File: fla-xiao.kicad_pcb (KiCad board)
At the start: 2 copper layers, 49.7 x 30.7 mm, 9 parts, among them J3 Conn_PinHeader_2x03_P2.54mm_V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, J4 Conn_PinHeader_1x08_P2.54mm_H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, J5 Conn_PinHeader_1x05_P2.54mm_H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, M1 Module_XIAO-RP2040_SocketSMD, SW1 BUTTON_B3SN

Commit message: Minor tweaks, updated image
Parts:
- moved R3 2.12 mm to (169.9, 150.7), turned to 0 degrees
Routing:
- net PWR_5V: track 52.5 -> 53.3 mm
- net PWR_3V3: track 114.2 -> 114.7 mm
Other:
- board size 49.7 x 30.7 mm -> 48.7 x 30.7 mm

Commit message: Fixed routing
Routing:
- net PWR_3V3: track 114.7 -> 115.3 mm
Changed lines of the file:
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@@
   (segment (start 164.979645 141.970355) (end 166.179199 141.970355) (width 0.6) (layer "F.Cu") (net 11))
   (segment (start 147.25 154) (end 145.39 152.14) (width 0.6) (layer "F.Cu") (net 12))
-  (segment (start 162 132.15) (end 162 134.035152) (width 0.6) (layer "F.Cu") (net 12))
-  (segment (start 168.9 129.35) (end 164.8 129.35) (width 0.6) (layer "F.Cu") (net 12))
+  (segment (start 162 134.035152) (end 161.404797 134.630355) (width 0.6) (layer "F.Cu") (net 12))
+  (segment (start 169.625 137.45) (end 169.625 129.775) (width 0.6) (layer "F.Cu") (net 12))
   (segment (start 148.675 130.625) (end 148.675 137.35) (width 0.6) (layer "F.Cu") (net 12))
   (segment (start 141.425 141.9) (end 143 141.9) (width 0.6) (layer "F.Cu") (net 12))
-  (segment (start 168.625 137.505) (end 168.625 145.85) (width 0.6) (layer "F.Cu") (net 12))
   (segment (start 168.504645 145.970355) (end 168.625 145.85) (width 0.6) (layer "F.Cu") (net 12))
   (segment (start 140.725 139.05) (end 140.725 141.2) (width 0.6) (layer "F.Cu") (net 12))
   (segment (start 147.725 138.3) (end 141.475 138.3) (width 0.6) (layer "F.Cu") (net 12))
   (segment (start 168.4 154) (end 147.25 154) (width 0.6) (layer "F.Cu") (net 12))
-  (segment (start 169.075 129.525) (end 168.9 129.35) (width 0.6) (layer "F.Cu") (net 12))
+  (segment (start 164.8 129.35) (end 162 132.15) (width 0.6) (layer "F.Cu") (net 12))
   (segment (start 145.39 150.9) (end 145.39 151.335) (width 0.6) (layer "F.Cu") (net 12))
   (segment (start 145.39 150.5) (end 145.39 150.9) (width 0.6) (layer "F.Cu") (net 12))
   (segment (start 148.675 137.35) (end 147.725 138.3) (width 0.6) (layer "F.Cu") (net 12))
   (segment (start 168.6125 148.3375) (end 169.8 149.525) (width 0.6) (layer "F.Cu") (net 12))
-  (segment (start 168.625 137.505) (end 169.075 137.055) (width 0.6) (layer "F.Cu") (net 12))
-  (segment (start 162 134.035152) (end 161.404797 134.630355) (width 0.6) (layer "F.Cu") (net 12))
   (segment (start 145.39 152.14) (end 145.39 150.9) (width 0.6) (layer "F.Cu") (net 12))
   (segment (start 168.625 148.325) (end 168.6125 148.3375) (width 0.6) (layer "F.Cu") (net 12))
   (segment (start 161.404799 134.630355) (end 161.414296 134.639854) (width 0.6) (layer "F.Cu") (net 12))
   (segment (start 141.475 138.3) (end 140.725 139.05) (width 0.6) (layer "F.Cu") (net 12))
-  (segment (start 164.8 129.35) (end 162 132.15) (width 0.6) (layer "F.Cu") (net 12))
   (segment (start 169.8 152.6) (end 168.4 154) (width 0.6) (layer "F.Cu") (net 12))
-  (segment (start 169.075 137.055) (end 169.075 129.525) (width 0.6) (layer "F.Cu") (net 12))
+  (segment (start 168.625 138.45) (end 169.625 137.45) (width 0.6) (layer "F.Cu") (net 12))
   (segment (start 133.495 134.88) (end 140.3 128.075) (width 0.6) (layer "F.Cu") (net 12))
   (segment (start 161.395298 134.639854) (end 161.404799 134.630355) (width 0.6) (layer "F.Cu") (net 12))
+  (segment (start 162 132.15) (end 162 134.035152) (width 0.6) (layer "F.Cu") (net 12))
   (segment (start 140.3 128.075) (end 146.125 128.075) (width 0.6) (layer "F.Cu") (net 12))
+  (segment (start 169.625 129.775) (end 169.2 129.35) (width 0.6) (layer "F.Cu") (net 12))
   (segment (start 140.725 141.2) (end 141.425 141.9) (width 0.6) (layer "F.Cu") (net 12))
   (segment (start 168.625 145.85) (end 168.625 148.325) (width 0.6) (layer "F.Cu") (net 12))
@@
   (segment (start 166.179199 145.970355) (end 168.504645 145.970355) (width 0.6) (layer "F.Cu") (net 12))
   (segment (start 132.7 134.88) (end 133.495 134.88) (width 0.6) (layer "F.Cu") (net 12))
+  (segment (start 169.2 129.35) (end 164.8 129.35) (width 0.6) (layer "F.Cu") (net 12))
   (segment (start 146.125 128.075) (end 148.675 130.625) (width 0.6) (layer "F.Cu") (net 12))
+  (segment (start 168.625 145.85) (end 168.625 138.45) (width 0.6) (layer "F.Cu") (net 12))
   (segment (start 139.375 126.8) (end 147.225 126.8) (width 0.6) (layer "F.Cu") (net 13))
   (segment (start 161.404797 129.550355) (end 160.825 130.130152) (width 0.6) (layer "F.Cu") (net 13))

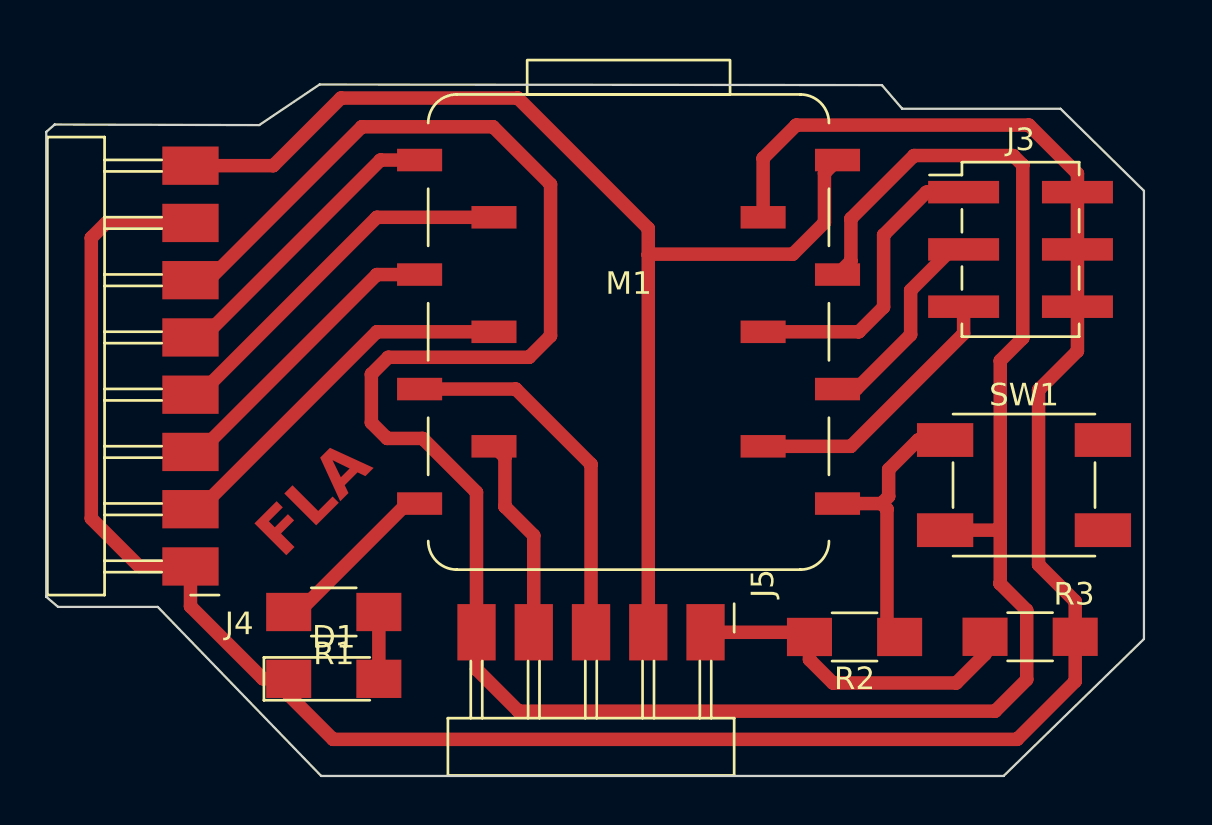
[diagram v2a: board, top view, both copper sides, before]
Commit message: Updated design, for Xtool Laser
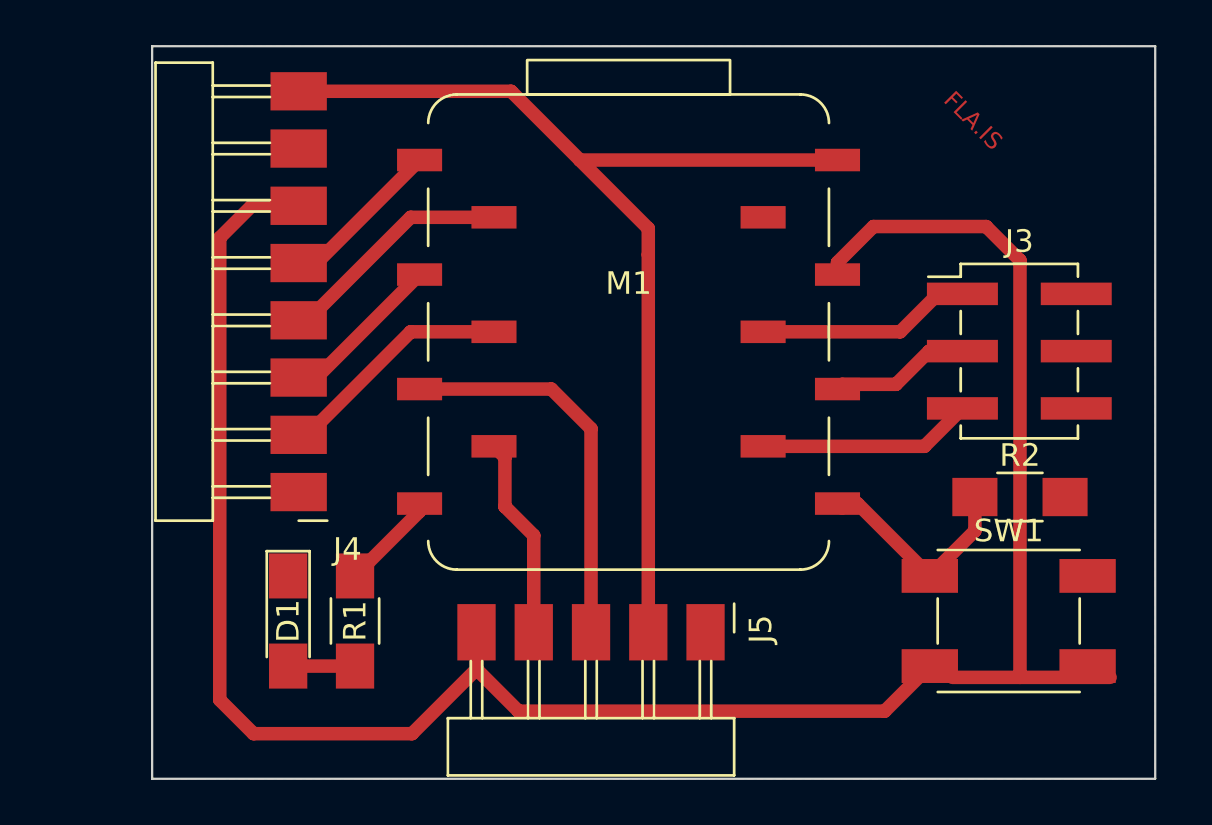
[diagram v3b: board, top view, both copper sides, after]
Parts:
- removed R3: R0, fab:R_1206
- R1: value 49.9 -> R1K
- moved R2 9.61 mm to (169.5, 144.5), turned to 0 degrees
- moved SW1 6.07 mm to (169.0, 150.0)
- moved J4 5.82 mm to (137.5, 144.3)
- moved J3 4.51 mm to (169.5, 138.0)
- moved D1 3.27 mm to (137.0, 150.0), turned to -90 degrees
- moved R1 1.02 mm to (140.0, 150.0), turned to 90 degrees
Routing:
- net GND: track 124.6 -> 0.00 mm
- net PWR_3V3: track 115.3 -> 97.0 mm
- net A2: track 13.4 -> 7.26 mm
- net A1: track 16.7 -> 10.6 mm
- net A0: track 13.4 -> 7.27 mm
- net A3: track 16.7 -> 10.6 mm
- net PWR_5V: track 53.3 -> 47.4 mm
- net A10: track 13.3 -> 9.54 mm
- net A6: track 7.80 -> 4.40 mm
- net A9: track 9.33 -> 6.25 mm
- net A7: track 12.9 -> 10.0 mm
- net A8: track 12.2 -> 9.54 mm
- net SDA: track 16.4 -> 17.4 mm
- added copper zone on F.Cu, net GND
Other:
- board size 48.7 x 30.7 mm -> 44.5 x 32.5 mm
- board text added: "FLA.IS"
- board text removed: "FLA"
